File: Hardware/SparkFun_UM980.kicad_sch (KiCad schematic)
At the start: 50 parts, among them J1 USB_C_Receptacle, U1 TVS_DIODE_ARRAY, U2 AP2112K-3.3, U5 UM980, U8 CH340C

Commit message: Remove old files
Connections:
- net D+: now reaches J1.A6 (D+), J1.B6 (D+), U1.6 (I/O4), U8.5 (UD+)
- net D-: now reaches J1.A7 (D-), J1.B7 (D-), U1.4 (I/O3), U8.6 (UD-)
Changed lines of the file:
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@@
+    (effects (font (size 1.27 1.27)) (justify left bottom))
+  )
+  (label "D+" (at 52.0636 41.91 0) (fields_autoplaced)
+    (effects (font (size 1.27 1.27)) (justify left bottom))
+  )
+  (label "D-" (at 52.07 44.45 0) (fields_autoplaced)
     (effects (font (size 1.27 1.27)) (justify left bottom))
   )

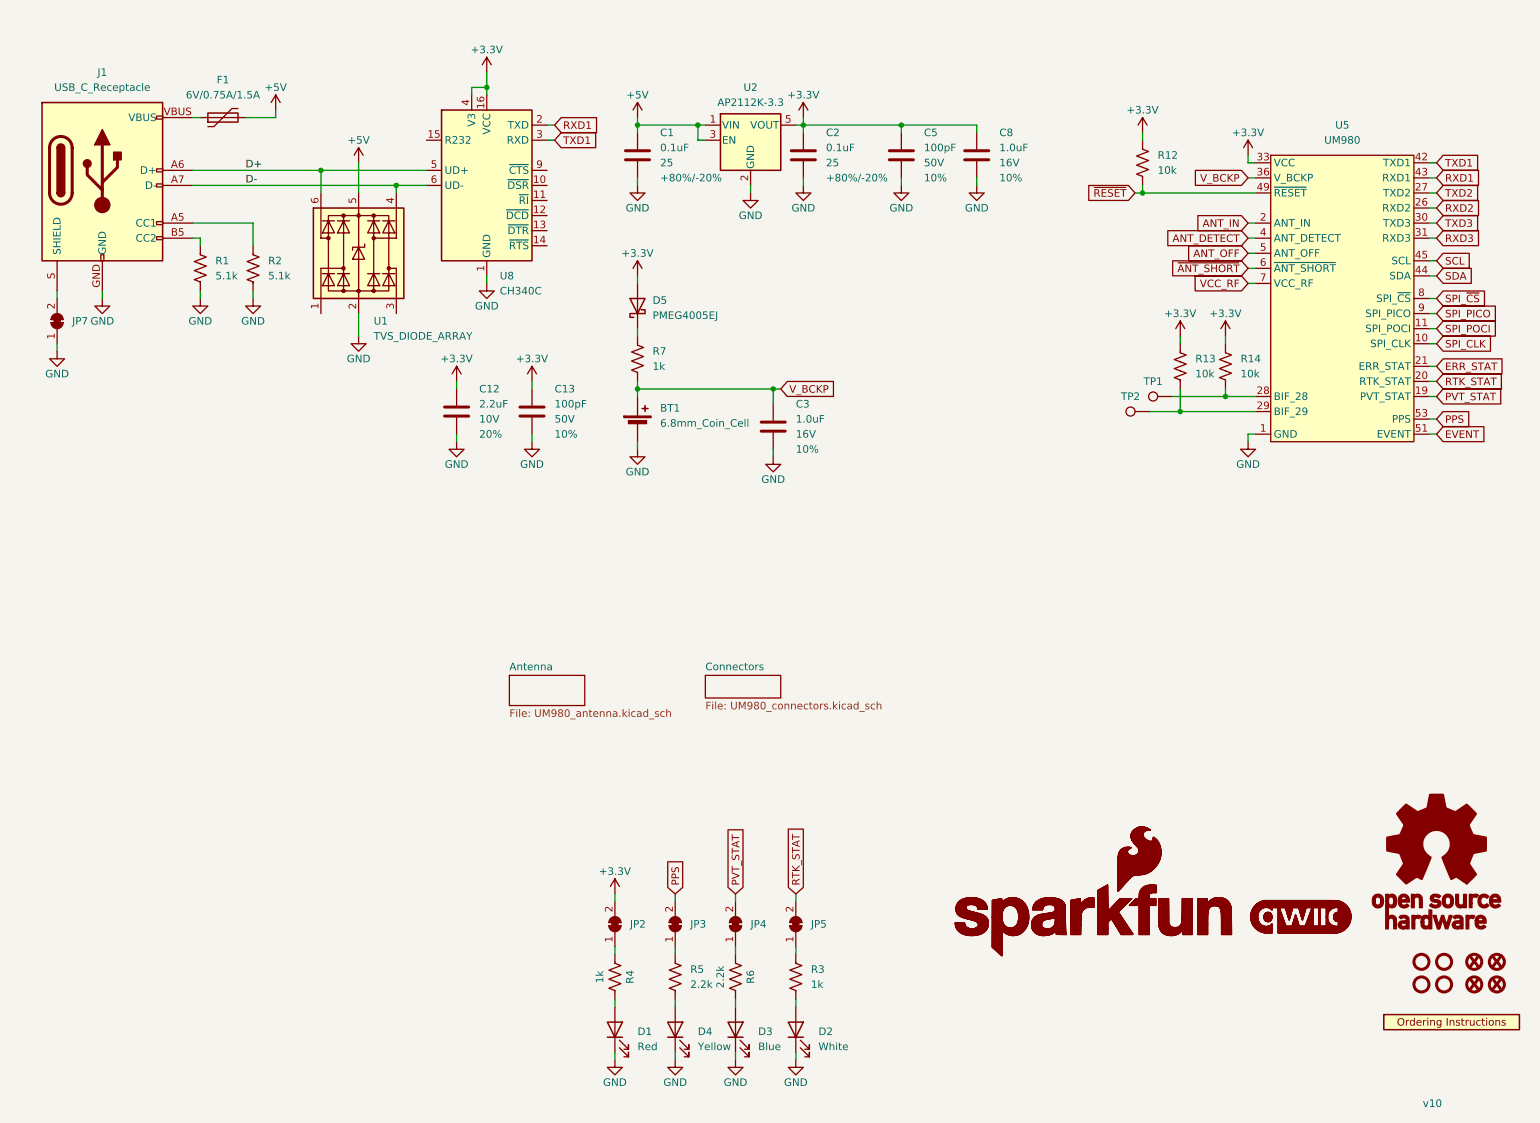
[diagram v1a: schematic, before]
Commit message: Add silk. Remove linked logos in sch.
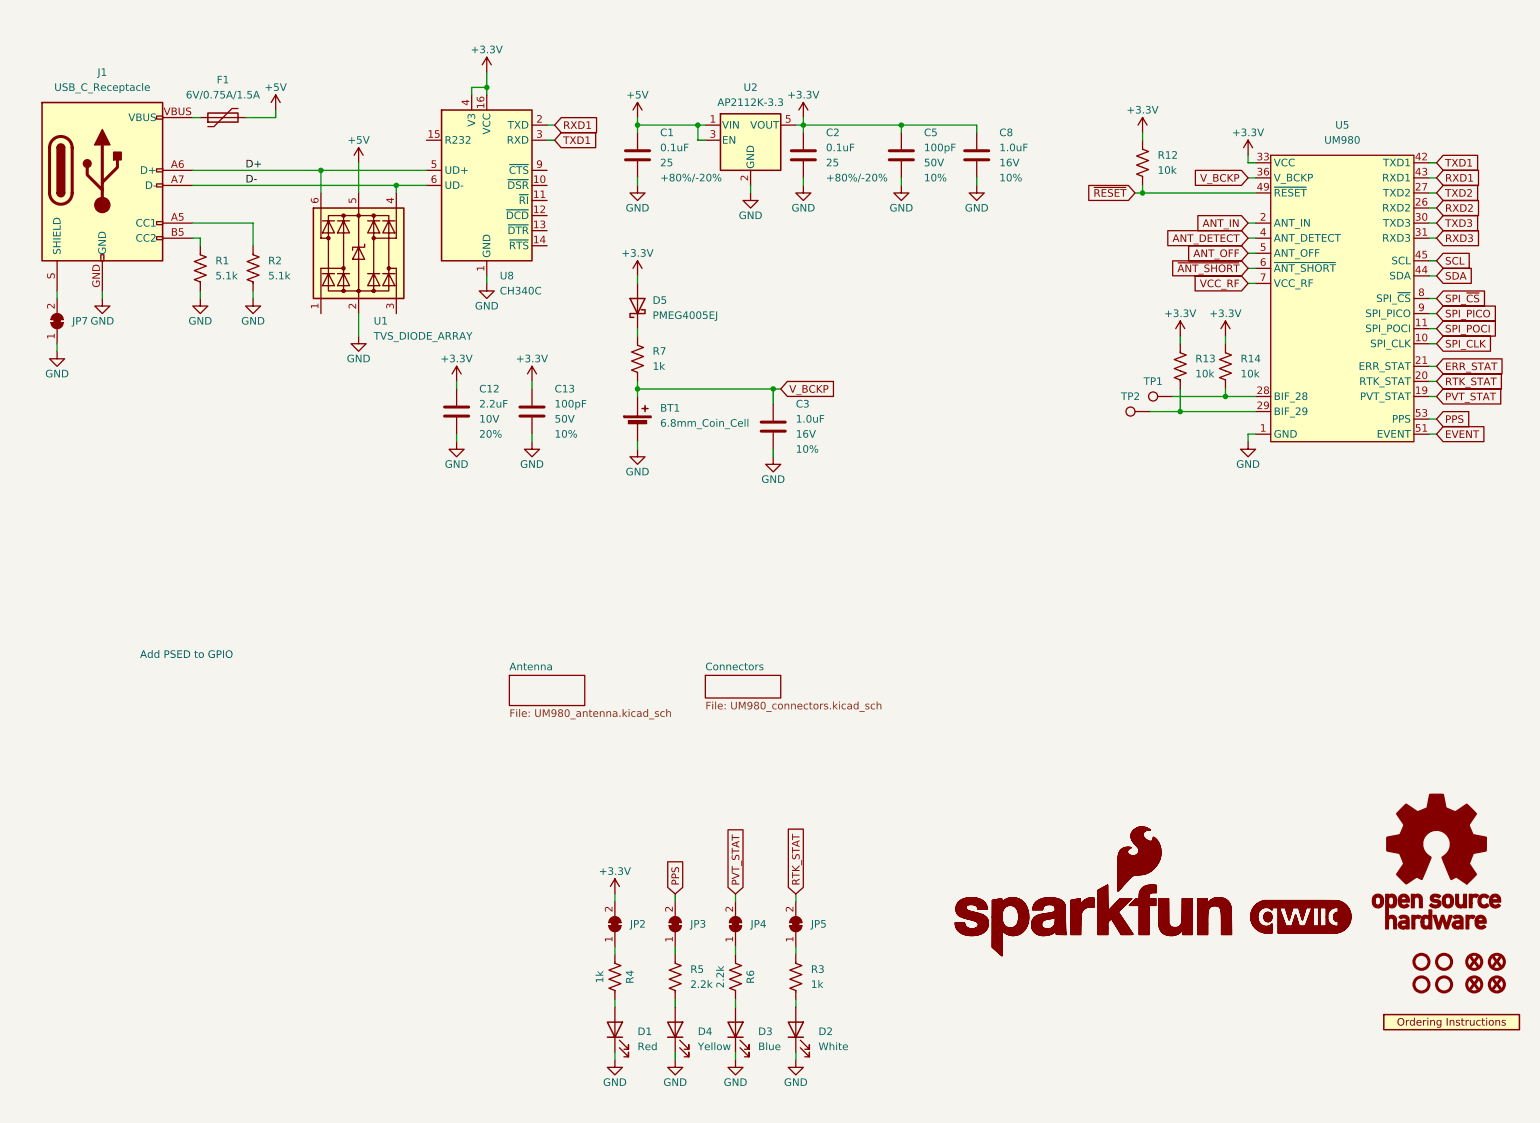
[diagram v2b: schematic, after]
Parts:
- G3: footprint SparkFun-Aesthetic:SparkFun_Logo_8mm -> (none)
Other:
- note added: "Add PSED to GPIO"
- note removed: "v10"
- title: (none) -> UM980 Triband GNSS Receiver Breakout
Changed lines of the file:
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@@
 (kicad_sch (version 20230121) (generator eeschema)
   (paper "USLetter")
+  (title_block
+    (title "UM980 Triband GNSS Receiver Breakout")
+    (date "2023-07-28")
+    (rev "v10")
+    (comment 1 "Designed by: N.Seidle")
+  )
   (junction (at 128.27 34.29) (diameter 0) (color 0 0 0 0)
   )
@@
     (stroke (width 0) (type default))
   )
-  (text "v10" (at 250.411 200.1093 0)
+  (text "Add PSED to GPIO" (at 34.29 124.46 0)
     (effects (font (size 1.27 1.27)) (justify left bottom))
   )
@@
   )
   (symbol (lib_id "SparkFun-Aesthetic:SparkFun_Logo") (at 194.31 167.64 0) (unit 1)
-    (in_bom yes) (on_board yes) (dnp no) (fields_autoplaced)
+    (in_bom yes) (on_board no) (dnp no) (fields_autoplaced)
     (property "Reference" "G5" (at 194.31 161.29 0)
       (effects (font (size 1.27 1.27)) hide)
@@
   )
   (symbol (lib_id "SparkFun-Aesthetic:SparkFun_Logo") (at 194.31 167.64 0) (unit 1)
-    (in_bom yes) (on_board yes) (dnp no) (fields_autoplaced)
+    (in_bom yes) (on_board no) (dnp no) (fields_autoplaced)
     (property "Reference" "G3" (at 194.31 161.29 0)
       (effects (font (size 1.27 1.27)) hide)
@@
       (effects (font (size 1.27 1.27)) hide)
     )
-    (property "Footprint" "SparkFun-Aesthetic:SparkFun_Logo_8mm" (at 198.123 163.8412 0)
-      (effects (font (size 1.27 1.27)) hide)
-    )
+    (property "Footprint" "" (at 198.123 163.8412 0)
+      (effects (font (size 1.27 1.27)) hide)
+    )

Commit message: Update design with PROD_IDs
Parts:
- removed G2, G4: LOGO, SparkFun-Aesthetic:qwiic_5.5mm, symbol SparkFun-Aesthetic:qwiic_Logo
- added C15, C17: 22uF, SparkFun-Capacitor:C_0603_1608Metric, symbol SparkFun-Capacitor:22uF_0603_6.3V_20%
- added C16: 0.1uF, SparkFun-Capacitor:C_0603_1608Metric, symbol SparkFun-Capacitor:0.1uF_0603_25V_20%
- added L2: 30Ω, SparkFun-Capacitor:C_0603_1608Metric, symbol SparkFun-Coil:30Ohm_100MHz_0603
- added R15, R16, R17, R18, R19, R20, R27, R28, R29, R30, R31, R32, R33, R34: 33, SparkFun-Resistor:R_0603_1608Metric, symbol SparkFun-Resistor:33_0603
- BT1: PROD_ID 14267 -> BATT-14267
- C1, C2: PROD_ID 810 -> CAP-00810
- C12: PROD_ID 7888 -> CAP-07888
- C13, C5: PROD_ID 7883 -> CAP-07883
- C3, C8: PROD_ID 13930 -> CAP-13930
- D1: PROD_ID 819 -> DIO-00819
- D2: PROD_ID 9004 -> DIO-09004
- D3: PROD_ID 8575 -> DIO-08575
- D4: PROD_ID 9003 -> DIO-09003
- D5: PROD_ID 10955 -> DIO-10955
- F1: PROD_ID 11150 -> RES-11150
- J1: PROD_ID (none) -> CONN-14122
- R1, R2: PROD_ID 12083 -> RES-12083
- R12, R13, R14: PROD_ID 824 -> RES-00824
- R3, R4, R7: PROD_ID 7856 -> RES-07856
- R5, R6: PROD_ID 8272 -> RES-08272
- U1: PROD_ID (none) -> IC-13538
- U2: PROD_ID (none) -> VREG-12457
- U5: PROD_ID (none) -> GPS-19527
- U8: PROD_ID IC-1234 -> IC-14038
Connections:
- net +3.3V: now also L2.1; no longer D5.A, R12.1, R13.1, R14.1, U5.33 (VCC), U5.34 (VCC)
- net ERR_STAT: now also R27.2; no longer U5.21 (ERR_STAT)
- net EVENT: now also R31.2; no longer U5.51 (EVENT)
- net GND: now also C15.2, C16.2, C17.2
- net PPS: now also R30.2; no longer U5.53 (PPS)
- net PVT_STAT: now also R29.2; no longer U5.19 (PVT_STAT)
- net RTK_STAT: now also R28.2; no longer U5.20 (RTK_STAT)
- net RXD1: now also R16.2; no longer U5.43 (RXD1)
- net RXD2: now also R18.2; no longer U5.26 (RXD2)
- net RXD3: now also R20.2; no longer U5.31 (RXD3)
- net TXD1: now also R15.2; no longer U5.42 (TXD1)
- net TXD2: now also R17.2; no longer U5.27 (TXD2)
- net TXD3: now also R19.2; no longer U5.30 (TXD3)
- net ~{RESET}: now also R34.2; no longer U5.49 (~{RESET})
- net SCL: no longer names the net of U5.45 (SCL)
- net SDA: no longer names the net of U5.44 (SDA)
- net SPI_CLK: no longer names the net of U5.10 (SPI_CLK)
- net SPI_PICO: no longer names the net of U5.9 (SPI_PICO)
- net SPI_POCI: no longer names the net of U5.11 (SPI_POCI)
- net SPI_~{CS}: no longer names the net of U5.8 (SPI_~{CS})
- new net: R13.2, R33.2, TP1.1
- new net: R30.1, U5.53 (PPS)
- new net: R28.1, U5.20 (RTK_STAT)
- new net: R15.1, U5.42 (TXD1)
- new net: R32.1, U5.28 (BIF_28)
- new net: R14.2, R32.2, TP2.1
- new net: R29.1, U5.19 (PVT_STAT)
- new net: R20.1, U5.31 (RXD3)
- new net: R27.1, U5.21 (ERR_STAT)
- new net: R17.1, U5.27 (TXD2)
- new net: U5.15 (NC), U5.16 (NC), U5.17 (NC), U5.18 (NC), U5.22 (NC), U5.23 (NC), U5.24 (NC), U5.25 (NC), U5.35 (NC), U5.38 (NC), U5.39 (NC), U5.40 (NC), U5.46 (NC), U5.47 (NC), U5.50 (NC), U5.52 (NC), U5.54 (NC)
- new net: R18.1, U5.26 (RXD2)
- new net: R33.1, U5.29 (BIF_29)
- new net: R19.1, U5.30 (TXD3)
- new net: R16.1, U5.43 (RXD1)
- new net: R34.1, U5.49 (~{RESET})
- new net: R31.1, U5.51 (EVENT)
- new net +3.3V_A: C15.1, C16.1, C17.1, D5.A, L2.2, R12.1, R13.1, R14.1, U5.33 (VCC), U5.34 (VCC)
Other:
- note added: "LEDs"
- note added: "Power"
- note added: "UM980 GNSS Triband"
- note removed: "Add PSED to GPIO"
- moved on the sheet: D1, D2, D3, D4, JP2, JP3, JP4, JP5, R3, R4, R5, R6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
